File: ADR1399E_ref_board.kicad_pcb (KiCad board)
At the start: 4 copper layers, 98 parts, among them J1 Conn_01x02_Pin, J2 USB_C_Receptacle_PowerOnly_6P, J3 Conn_Coaxial, J4 S4B-XH-A, P1 JST_B2P_VH, Q1 MMBT3906, U1 LT3042xMSE, U2 TPS61085DGK, U3 OPA182IDR, U4 OPA994IDR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

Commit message: interV1
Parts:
- moved TP2 71.5 mm to (49.8, 113.5)
- moved P1 69.8 mm to (140.2, 50.5)
- moved TP1 68.6 mm to (64.9, 107.8)
- moved C11 67.5 mm to (53.6, 78.8), turned to -90 degrees
- moved D4 50.8 mm to (49.9, 101.0), turned to 0 degrees
- moved R8 49.1 mm to (62.2, 80.1), turned to -90 degrees
- moved R29 43.9 mm to (49.8, 104.1), turned to 180 degrees
- moved R3 39.3 mm to (62.2, 76.3), turned to -90 degrees
- moved R9 35.6 mm to (56.2, 70.5), turned to 180 degrees
- moved TP5 34.9 mm to (51.3, 83.7)
- moved TP6 32.1 mm to (33.9, 102.9)
- moved TP3 18.0 mm to (66.6, 118.3)
- moved C10 16.2 mm to (58.4, 85.7)
- moved R11 14.9 mm to (92.5, 62.1)
- moved R12 14.9 mm to (92.5, 65.0)
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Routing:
- net Net-(D6-A): track 8.54 -> 32.4 mm
- net /Inductance: track 0.00 -> 21.5 mm
- net Net-(U5--): track 0.00 -> 12.0 mm
- net Net-(U1-PG): track 0.00 -> 8.76 mm, vias 0 -> 2
- net +BATT: track 0.00 -> 7.91 mm
- net Net-(D4-A): track 0.00 -> 4.47 mm
- net Net-(R19-Pad2): track 0.00 -> 3.36 mm
- net GND: vias 0 -> 3
- net +12V: vias 0 -> 6
- added copper zone on B.Cu, net +12V
- added copper zone on F.Cu, net +12V
- added copper zone on F.Cu, net +BATT
- added copper zone on F.Cu, net /Inductance
- added copper zone on B.Cu, net GND
- added copper zone on F.Cu, net Net-(C11-Pad1)
- added copper zone on F.Cu, net Net-(D6-K)
- added copper zone on F.Cu, net Net-(U1-OUTS)
- added copper zone on F.Cu, net Net-(U1-PGFB)
- added copper zone on F.Cu, net Net-(U1-SET)
- removed copper zone on In1.Cu, net GND
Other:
- board outline added: 149 x 66 mm

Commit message: maybe power done
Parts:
- added REF**: MountingHole_3.5mm, MountingHole:MountingHole_3.5mm, F.Cu at (35.5, 78.0)
- moved J3 109.6 mm to (145.2, 104.0), turned to 180 degrees
- moved C15 99.4 mm to (104.9, 107.3)
- moved C16 98.1 mm to (103.5, 109.3), turned to 180 degrees
- moved C22 97.2 mm to (92.4, 113.3), turned to 180 degrees
- moved C21 88.4 mm to (93.9, 98.8), turned to 180 degrees
- moved R22 76.8 mm to (89.9, 98.8), turned to 180 degrees
- moved U6 76.3 mm to (92.5, 103.8), turned to 90 degrees
- moved REF** 75.0 mm to (36.0, 129.5)
- moved TP4 20.8 mm to (70.0, 76.5)
- moved R11 17.4 mm to (82.3, 76.2)
- moved R9 15.5 mm to (50.2, 84.8), turned to -90 degrees
- moved TP5 13.2 mm to (61.0, 92.6), turned to 90 degrees
- moved C13 11.6 mm to (53.5, 85.0), turned to -90 degrees
- moved C11 9.88 mm to (58.5, 87.4), turned to 0 degrees
- moved C10 7.57 mm to (65.3, 82.6), turned to 90 degrees
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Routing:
- net Net-(U1-PG): track 8.76 -> 12.7 mm
- net Net-(D3-A): track 0.05 -> 3.66 mm
- net Net-(U5--): track 12.0 -> 9.68 mm
- net /Inductance: track 21.5 -> 19.5 mm
- net Net-(D6-A): track 32.4 -> 34.2 mm
- net +BATT: track 7.91 -> 6.22 mm
- net Net-(J2-CC2): track 5.36 -> 6.48 mm
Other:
- board size 149 x 66 mm -> 119 x 60 mm

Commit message: Reference Island formed!
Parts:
- removed C22: 1uF 25V, Capacitor_SMD:C_0603_1608Metric_Pad1.08x0.95mm_HandSolder
- removed REF** (x2): MountingHole_3.5mm, MountingHole:MountingHole_3.5mm
- added H1: MountingHole, MountingHole:MountingHole_3.2mm_M3_ISO7380, F.Cu at (22.9, 87.7)
- added H2: MountingHole, MountingHole:MountingHole_3.2mm_M3_ISO7380, F.Cu at (22.9, 94.9)
- added H3: MountingHole, MountingHole:MountingHole_3.2mm_M3_ISO7380, F.Cu at (22.9, 102.2)
- added H4: MountingHole, MountingHole:MountingHole_3.2mm_M3_ISO7380, F.Cu at (22.9, 109.4)
- added H5: MountingHole, MountingHole:MountingHole_2.2mm_M2, F.Cu at (81.0, 90.0)
- added H6: MountingHole, MountingHole:MountingHole_2.2mm_M2, F.Cu at (102.5, 90.0)
- added H7: MountingHole, MountingHole:MountingHole_2.2mm_M2, F.Cu at (102.5, 118.0)
- added H8: MountingHole, MountingHole:MountingHole_2.2mm_M2, F.Cu at (81.0, 118.0)
- moved C16 17.4 mm to (89.1, 99.5)
- moved C15 14.0 mm to (93.2, 99.5)
- moved C21 9.37 mm to (95.7, 108.0), turned to 90 degrees
- moved R22 7.80 mm to (95.7, 104.0), turned to 90 degrees
- moved U6 1.42 mm to (91.2, 104.3), turned to -90 degrees
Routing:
- net GND: track 0.00 -> 23.7 mm, vias 3 -> 9
- net Net-(U4-V+): track 0.00 -> 19.5 mm
- net /Vref: track 0.00 -> 18.9 mm
- net Net-(C21-Pad2): track 0.00 -> 2.21 mm
- net /Inductance: track 19.5 -> 18.9 mm
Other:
- outline, holes or cut-outs redrawn

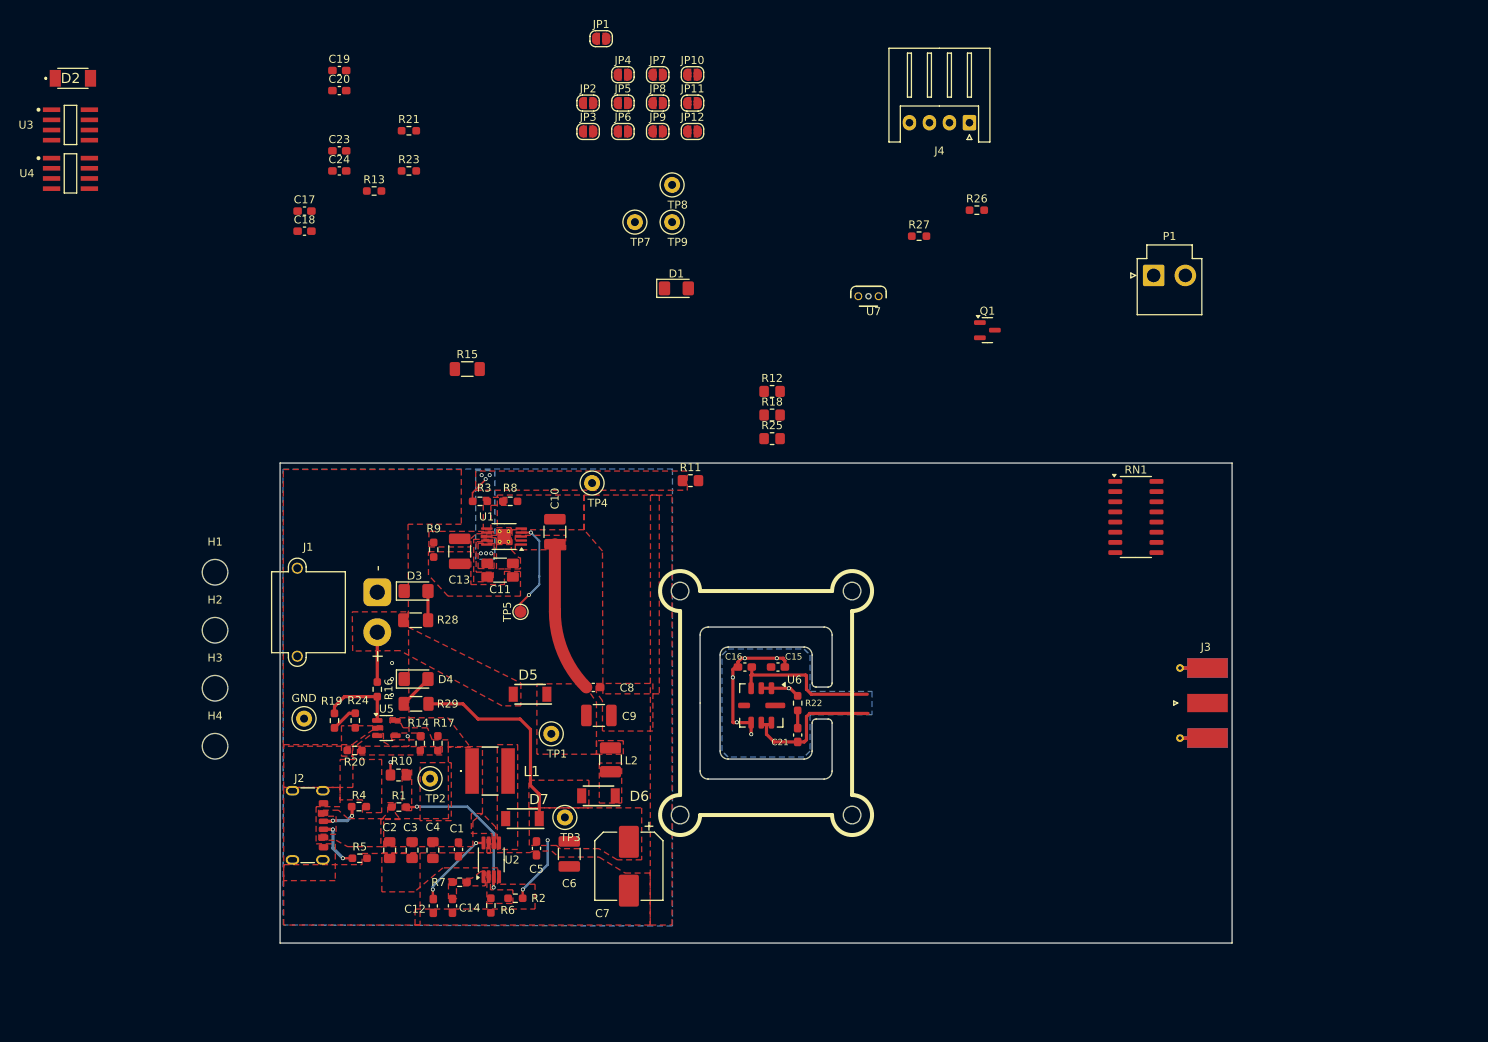
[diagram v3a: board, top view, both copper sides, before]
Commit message: initial amp placement
initial amp placement
Added Vbatt divider
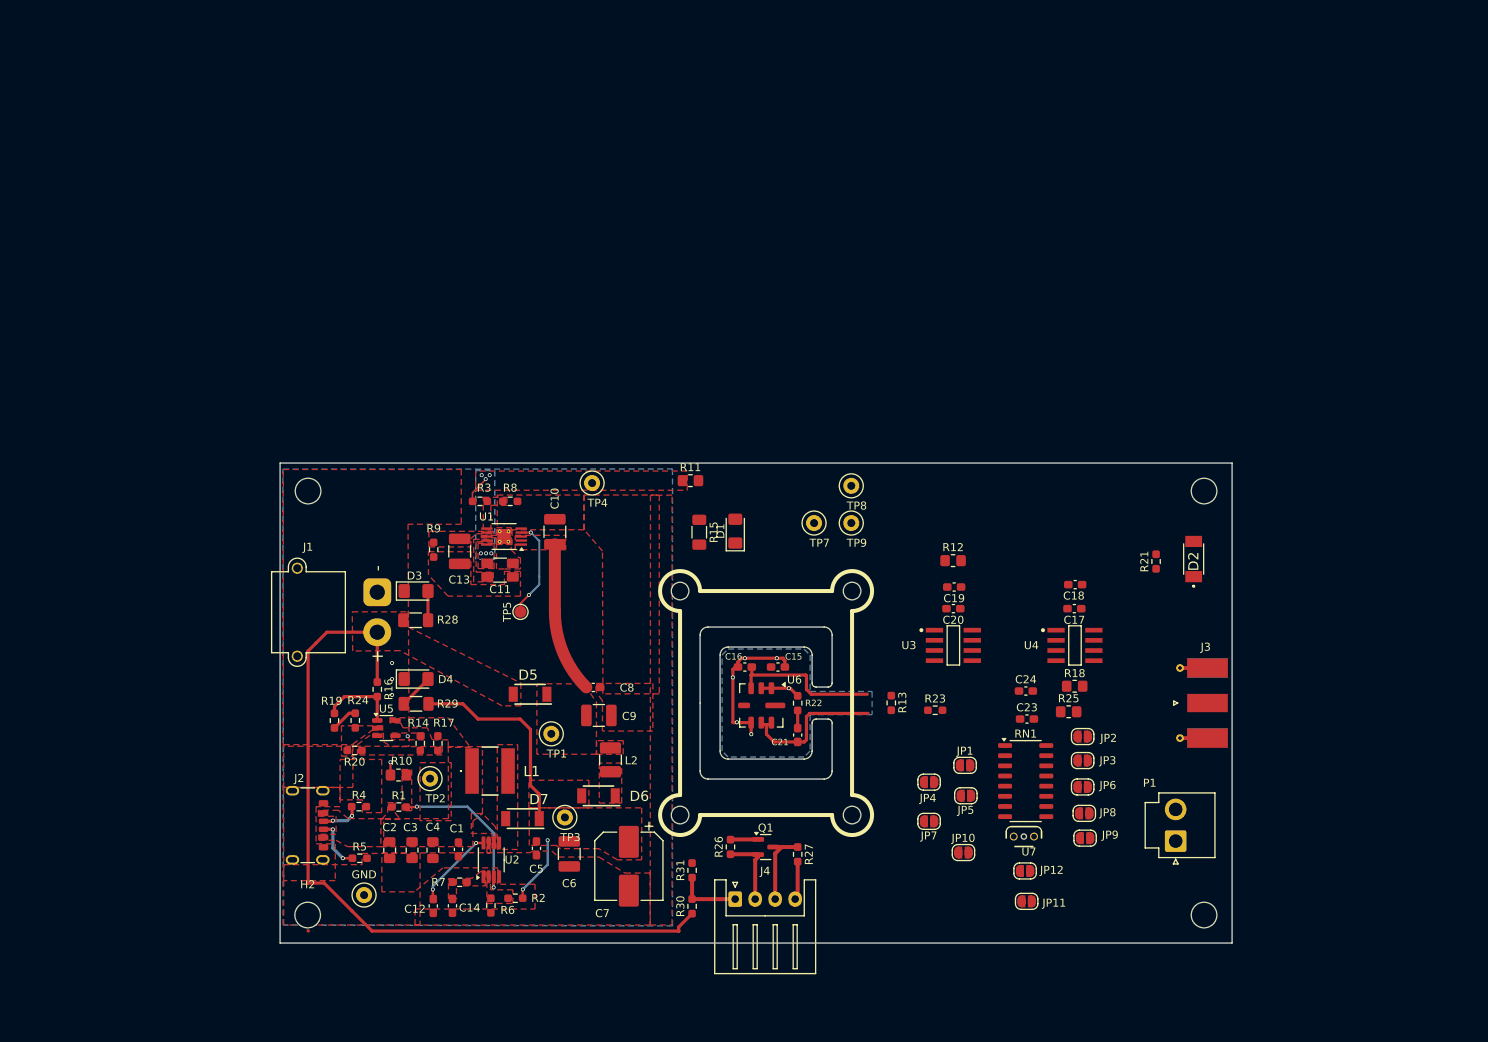
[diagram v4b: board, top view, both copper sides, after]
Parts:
- added R30: 120k 0.1%, Resistor_SMD:R_0603_1608Metric_Pad0.98x0.95mm_HandSolder, F.Cu at (82.5, 129.4)
- added R31: 17.8k 0.1%, Resistor_SMD:R_0603_1608Metric_Pad0.98x0.95mm_HandSolder, F.Cu at (82.5, 124.9)
- moved D2 152.4 mm to (145.2, 86.0), turned to 90 degrees
- moved U4 138.7 mm to (130.4, 96.8)
- moved U3 128.1 mm to (115.2, 96.8)
- moved H3 126.1 mm to (146.5, 77.5)
- moved H4 125.4 mm to (146.5, 130.5)
- moved C23 111.5 mm to (124.4, 106.0)
- moved C17 108.3 mm to (130.3, 92.2), turned to 180 degrees
- moved JP11 108.2 mm to (124.3, 128.8)
- moved R21 107.8 mm to (140.5, 86.3), turned to 90 degrees
- moved C24 107.7 mm to (124.2, 102.5)
- moved C18 106.0 mm to (130.4, 89.2), turned to 180 degrees
- moved JP8 103.6 mm to (131.5, 117.8)
- moved JP9 103.2 mm to (131.6, 120.9)
- moved JP10 103.0 mm to (116.4, 122.7)
- moved JP1 101.6 mm to (116.6, 111.8)
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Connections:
- net Net-(J4-Pin_2) renamed /LMT_VCC
- net Net-(J4-Pin_3) renamed /LMT_OUT
- net Net-(U4-V+) renamed /12V_Out
- J1 pad : (no net) -> GND
- J4 pad 1: unconnected-(J4-Pin_1-Pad1) -> /VBATT_MEAS
- J4 pad 4: GNDREF -> GND
- R27 pad 2: GNDREF -> GND
- U7 pad 1: GNDREF -> GND
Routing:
- net +BATT: track 6.22 -> 96.6 mm
- net /LMT_OUT: track 0.00 -> 9.91 mm
- net /LMT_VCC: track 0.00 -> 9.20 mm
- net /VBATT_MEAS: track 0.00 -> 8.07 mm
- net GND: track 23.7 -> 28.6 mm
- net Net-(Q1-B): track 0.00 -> 3.47 mm

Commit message: getting closer
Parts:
- J4: footprint Connector_JST:JST_XH_S4B-XH-A_1x04_P2.50mm_Horizontal -> Connector_JST:JST_XH_S4B-XH-A-1_1x04_P2.50mm_Horizontal
- moved TP8 54.2 mm to (139.0, 116.8)
- moved TP7 45.1 mm to (141.0, 94.4)
- moved P1 33.5 mm to (137.3, 88.3)
- moved R21 18.6 mm to (140.3, 104.9), turned to -90 degrees
- moved TP9 15.0 mm to (110.0, 94.4)
- moved R25 7.27 mm to (136.6, 103.2)
- moved C24 6.95 mm to (117.3, 103.4)
- moved R18 6.59 mm to (136.5, 99.6)
- moved C18 4.40 mm to (127.6, 92.6)
- moved C17 3.88 mm to (127.6, 95.0)
- moved U4 3.58 mm to (127.5, 99.0)
- moved JP11 3.51 mm to (121.8, 126.4)
- moved JP12 3.23 mm to (121.8, 122.8)
- moved JP10 3.22 mm to (114.7, 120.0)
- moved C19 2.96 mm to (114.7, 92.4)
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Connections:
- J1 pad : GND -> (no net)
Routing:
- net /10V_Out: track 0.00 -> 45.4 mm, vias 0 -> 2
- net Net-(Q1-B): track 3.47 -> 36.9 mm, vias 0 -> 1
- net Net-(JP11-B): track 0.00 -> 24.8 mm
- net Net-(JP1-B): track 0.00 -> 24.1 mm, vias 0 -> 2
- net /12V_Out: track 19.5 -> 41.2 mm
- net Net-(JP12-A): track 0.00 -> 21.5 mm, vias 0 -> 2
- net /Vref: track 18.9 -> 39.4 mm
- net Net-(RN1-R1.1): track 0.00 -> 18.0 mm
- net Net-(RN1-R1.2): track 0.00 -> 16.3 mm
- net Net-(JP10-A): track 0.00 -> 14.6 mm
- net GND: track 28.6 -> 42.0 mm, vias 9 -> 79
- net Net-(JP1-A): track 0.00 -> 12.9 mm
- net Net-(U3-OUT): track 0.00 -> 12.3 mm
- net Net-(U3-V+): track 0.00 -> 11.0 mm
- net Net-(U4--IN): track 0.00 -> 10.9 mm
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- added copper zone on In2.Cu, net +12V
- added copper zone on F.Cu, net /10V_Out
- added copper zone on F.Cu, net /12V_Out
- added copper zone on In1.Cu, net GND
- removed copper zone on B.Cu, net +12V
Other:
- board text added: "+12V"
- board text added: "+5V"
- board text added: "GND"
- board text added: "PG"
- board text added: "V_10V"
- board text added: "V_REF"

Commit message: cleanup
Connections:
- J1 pad : (no net) -> GND
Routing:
- net /12V_Out: track 41.2 -> 42.2 mm
- net GND: vias 79 -> 291

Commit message: more cleanup
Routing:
- net Net-(JP12-A): track 21.5 -> 23.1 mm
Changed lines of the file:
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@@
 		(sheetfile "ADR1399E_ref_board.kicad_sch")
 		(zone_connect 2)
-		(attr smd)
 		(fp_line
 			(start 2.5 0.25)
@@
 			)
 		)
-		(pad "1" smd rect
+		(pad "1" connect rect
 			(at -1.72 0 180)
 			(size 5.08 2.29)
-			(layers "F.Cu" "F.Mask" "F.Paste")
+			(layers "F.Cu" "F.Mask")
 			(net 20 "/10V_Out")
 			(pinfunction "In")
 			(pintype "passive")
 		)
-		(pad "2" smd rect
+		(pad "2" connect rect
 			(at -1.72 -4.38 180)
 			(size 5.08 2.42)
-			(layers "F.Cu" "F.Mask" "F.Paste")
+			(layers "F.Cu" "F.Mask")
 			(net 1 "GND")
 			(pinfunction "Ext")
 			(pintype "passive")
 		)
-		(pad "2" smd rect
+		(pad "2" connect rect
 			(at -1.72 -4.38 180)
 			(size 5.08 2.42)
-			(layers "B.Cu" "B.Mask" "B.Paste")
+			(layers "B.Cu" "B.Mask")
 			(net 1 "GND")
 			(pinfunction "Ext")
 			(pintype "passive")
 		)
-		(pad "2" smd rect
+		(pad "2" connect rect
 			(at -1.72 4.38 180)
 			(size 5.08 2.42)
-			(layers "F.Cu" "F.Mask" "F.Paste")
+			(layers "F.Cu" "F.Mask")
 			(net 1 "GND")
 			(pinfunction "Ext")
 			(pintype "passive")
 		)
-		(pad "2" smd rect
+		(pad "2" connect rect
 			(at -1.72 4.38 180)
 			(size 5.08 2.42)
-			(layers "B.Cu" "B.Mask" "B.Paste")
+			(layers "B.Cu" "B.Mask")
 			(net 1 "GND")
 			(pinfunction "Ext")
@@
 	)
 	(segment
+		(start 117.7 119.7)
+		(end 117.7 116.9)
+		(width 0.5)
+		(layer "F.Cu")
+		(net 26)
+	)
+	(segment
 		(start 121.1 122.8)
 		(end 119.4 122.8)
@@
 	)
 	(segment
+		(start 117.7 116.9)
+		(end 117.7 118.5)
+		(width 0.5)
+		(layer "F.Cu")
+		(net 26)
+	)
+	(segment
 		(start 117.7 121.1)
 		(end 117.7 119.7)
@@
 	)
 	(via
-		(at 117.7 119.7)
+		(at 117.7 116.9)
 		(size 0.5)
 		(drill 0.3)
@@
 	)
 	(segment
-		(start 117.7 119.7)
-		(end 117.7 114.45)
+		(start 117.7 114.45)
+		(end 117.7 116.9)
 		(width 0.5)
 		(layer "In2.Cu")
@@
 		(polygon
 			(pts
-				(xy 115 118.5) (xy 117 116) (xy 123.5 116) (xy 123 122.5) (xy 117.5 122.5)
+				(xy 112.6 118.3) (xy 112.7 113.8) (xy 130 113.8) (xy 130.2 120.7) (xy 117.9 124.1)
 			)
 		)

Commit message: copper balancing
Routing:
- net Net-(JP12-A): track 23.1 -> 21.5 mm
- net GND: vias 291 -> 311
- added copper zone on B.Cu, net +12V
- added copper zone on In2.Cu, net GND
- removed copper zone on In2.Cu, net +12V
